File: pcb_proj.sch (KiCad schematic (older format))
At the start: 0 parts

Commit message: Mi-work push
Started dropping in the op-amps, still work in progress.
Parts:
- added R5: 1k, symbol R
- added U0, U1, U2, U3, U4, U5, U6, U7, U8, U9: OPA333xxDBV, symbol OPA333xxDBV
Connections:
- net labels added: GNDA, crossbar_out5, crossbar_out5_-v
- net labels removed: +12L
- wire segments 0 -> 8
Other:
- note added: "<--Ip--"
- note added: "Rf"
- note added: "Vout"
- note added: "Vout = Ip * Rf"
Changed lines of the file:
@@
 encoding utf-8
 Sheet 1 1
-Title ""
-Date ""
+Title "Operational Amplifiers"
+Date "2019-02-18"
 Rev ""
-Comp ""
+Comp "Emulating NN with Resistor Network"
 Comment1 ""
 Comment2 ""
@@
 $EndDescr
 $Comp
-L +12L #PWR?
-U 1 1 5C608EB0
-P 8050 2800
-F 0 "#PWR?" H 8050 2650 50  0001 C CNN
-F 1 "+12L" H 8050 2940 50  0000 C CNN
-F 2 "" H 8050 2800 50  0001 C CNN
-F 3 "" H 8050 2800 50  0001 C CNN
-	1    8050 2800
+L OPA333xxDBV U4
+U 1 1 5C6B1C00
+P 8750 3050
+F 0 "U4" H 8750 3250 50  0000 L CNN
+F 1 "OPA333xxDBV" H 8750 2850 50  0000 L CNN
+F 2 "" H 8750 3050 50  0001 C CNN
+F 3 "" H 8750 3250 50  0001 C CNN
+	1    8750 3050
 	1    0    0    -1
 $EndComp
+$Comp
+L OPA333xxDBV U5
+U 1 1 5C6B1C2C
+P 2500 4850
+F 0 "U5" H 2500 5050 50  0000 L CNN
+F 1 "OPA333xxDBV" H 2500 4650 50  0000 L CNN
+F 2 "" H 2500 4850 50  0001 C CNN
+F 3 "" H 2500 5050 50  0001 C CNN
+	1    2500 4850
+	1    0    0    -1
+$EndComp
+$Comp
+L OPA333xxDBV U7
+U 1 1 5C6B1C4E
+P 5500 4850
+F 0 "U7" H 5500 5050 50  0000 L CNN
+F 1 "OPA333xxDBV" H 5500 4650 50  0000 L CNN
+F 2 "" H 5500 4850 50  0001 C CNN
+F 3 "" H 5500 5050 50  0001 C CNN
+	1    5500 4850
+	1    0    0    -1
+$EndComp
+$Comp
+L OPA333xxDBV U9
+U 1 1 5C6B1C6F
+P 8750 4950
+F 0 "U9" H 8750 5150 50  0000 L CNN
+F 1 "OPA333xxDBV" H 8750 4750 50  0000 L CNN
+F 2 "" H 8750 4950 50  0001 C CNN
+F 3 "" H 8750 5150 50  0001 C CNN
+	1    8750 4950
+	1    0    0    -1
+$EndComp
+$Comp
+L OPA333xxDBV U2
+U 1 1 5C6B1C93
+P 5500 3000
+F 0 "U2" H 5500 3200 50  0000 L CNN
+F 1 "OPA333xxDBV" H 5500 2800 50  0000 L CNN
+F 2 "" H 5500 3000 50  0001 C CNN
+F 3 "" H 5500 3200 50  0001 C CNN
+	1    5500 3000
+	1    0    0    -1
+$EndComp
+$Comp
+L OPA333xxDBV U3
+U 1 1 5C6B1CC4
+P 7150 3000
+F 0 "U3" H 7150 3200 50  0000 L CNN
+F 1 "OPA333xxDBV" H 7150 2800 50  0000 L CNN
+F 2 "" H 7150 3000 50  0001 C CNN
+F 3 "" H 7150 3200 50  0001 C CNN
+	1    7150 3000
+	1    0    0    -1
+$EndComp
+$Comp
+L OPA333xxDBV U6
+U 1 1 5C6B1CF6
+P 4000 4850
+F 0 "U6" H 4000 5050 50  0000 L CNN
+F 1 "OPA333xxDBV" H 4000 4650 50  0000 L CNN
+F 2 "" H 4000 4850 50  0001 C CNN
+F 3 "" H 4000 5050 50  0001 C CNN
+	1    4000 4850
+	1    0    0    -1
+$EndComp
+$Comp
+L OPA333xxDBV U8
+U 1 1 5C6B1D2B
+P 7150 4850
+F 0 "U8" H 7150 5050 50  0000 L CNN
+F 1 "OPA333xxDBV" H 7150 4650 50  0000 L CNN
+F 2 "" H 7150 4850 50  0001 C CNN
+F 3 "" H 7150 5050 50  0001 C CNN
+	1    7150 4850
+	1    0    0    -1
+$EndComp
+$Comp
+L OPA333xxDBV U1
+U 1 1 5C6B1D5D
+P 4050 3000
+F 0 "U1" H 4050 3200 50  0000 L CNN
+F 1 "OPA333xxDBV" H 4050 2800 50  0000 L CNN
+F 2 "" H 4050 3000 50  0001 C CNN
+F 3 "" H 4050 3200 50  0001 C CNN
+	1    4050 3000
+	1    0    0    -1
+$EndComp
+$Comp
+L OPA333xxDBV U0
+U 1 1 5C6B1D94
+P 2500 3000
+F 0 "U0" H 2500 3200 50  0000 L CNN
+F 1 "OPA333xxDBV" H 2500 2800 50  0000 L CNN
+F 2 "" H 2500 3000 50  0001 C CNN
+F 3 "" H 2500 3200 50  0001 C CNN
+	1    2500 3000
+	1    0    0    -1
+$EndComp
+$Comp
+L GNDA #PWR?
+U 1 1 5C6B2BDA
+P 2200 5400
+F 0 "#PWR?" H 2200 5150 50  0001 C CNN
+F 1 "GNDA" H 2200 5250 50  0000 C CNN
+F 2 "" H 2200 5400 50  0001 C CNN
+F 3 "" H 2200 5400 50  0001 C CNN
+	1    2200 5400
+	1    0    0    -1
+$EndComp
+Wire Wire Line
+	2200 4950 2200 5400
+Text GLabel 1550 4750 0    60   Input ~ 0
+crossbar_out5
+$Comp
+L R R5
+U 1 1 5C6B34F2
+P 2250 4150
+F 0 "R5" V 2330 4150 50  0000 C CNN
+F 1 "1k" V 2250 4150 50  0000 C CNN
+F 2 "" V 2180 4150 50  0001 C CNN
+F 3 "" H 2250 4150 50  0001 C CNN
+	1    2250 4150
+	0    1    1    0
+$EndComp
+Wire Wire Line
+	1550 4750 2200 4750
+Wire Wire Line
+	1800 4750 1800 4150
+Wire Wire Line
+	1800 4150 2100 4150
+Connection ~ 1800 4750
+Wire Wire Line
+	2400 4150 2800 4150
+Wire Wire Line
+	2800 4150 2800 4850
+Wire Wire Line
+	2800 4850 3150 4850
+Wire Wire Line
+	3150 4850 3150 5350
+Connection ~ 2800 4850
+Text GLabel 3150 5350 0    60   Input ~ 0
+crossbar_out5_-v
+Text Notes 1150 4000 0    60   ~ 0
+Vout = Ip * Rf
+Text Notes 2950 4850 0    60   ~ 0
+Vout
+Text Notes 2500 4150 0    60   ~ 0
+Rf
+Text Notes 2050 4050 0    60   ~ 0
+<--Ip--
 $EndSCHEMATC

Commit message: About to make a heirarchy, committing first in case we need to go back
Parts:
- added R0, R1, R2, R3, R4, R6, R7, R8, R9: 1k, symbol R
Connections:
- net GNDA is gone; now on net GND: U5.4 (-)
- net crossbar_out4_-v: now reaches U4.1
- net crossbar_out4_-v: now also R4.1
- net crossbar_out3: now reaches U4.3 (+)
- net crossbar_out3: now also U3.3 (+), R3.2, R4.2
- net GND: now reaches U4.4 (-)
- net GND: now also U0.4 (-), U1.4 (-), U2.4 (-), U3.4 (-), U6.4 (-), U7.4 (-), U8.4 (-), U9.4 (-)
- net crossbar_out7_-v: now reaches U7.1
- net crossbar_out7_-v: now also R7.1
- net crossbar_out7: now reaches U7.3 (+)
- net crossbar_out7: now also R7.2
- net crossbar_out9_-v: now reaches U9.1
- net crossbar_out9_-v: now also R9.1
- net crossbar_out9: now reaches U9.3 (+)
- net crossbar_out9: now also R9.2
- net crossbar_out2_-v: now reaches U2.1
- net crossbar_out2_-v: now also R2.1
- net crossbar_out2: now reaches U2.3 (+)
- net crossbar_out2: now also R2.2
- net crossbar_out3_-v: now reaches U3.1
- net crossbar_out3_-v: now also R3.1
- net crossbar_out6_-v: now reaches U6.1
- net crossbar_out6_-v: now also R6.1
- net crossbar_out6: now reaches U6.3 (+)
- net crossbar_out6: now also R6.2
- net crossbar_out8_-v: now reaches U8.1
- net crossbar_out8_-v: now also R8.1
- net crossbar_out8: now reaches U8.3 (+)
- net crossbar_out8: now also R8.2
- net crossbar_out1_-v: now reaches U1.1
- net crossbar_out1_-v: now also R1.1
- net crossbar_out1: now reaches U1.3 (+)
- net crossbar_out1: now also R1.2
- net crossbar_out0_-v: now reaches U0.1
- net crossbar_out0_-v: now also R0.1
- net crossbar_out0: now reaches U0.3 (+)
- net crossbar_out0: now also R0.2
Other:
- note added: "This op amp is wired the same as the rest, just more\nexplicit in what's going on. Note the output voltage \nwill appear negative if the current is going INTO the \n1k resistor."
- moved on the sheet: R5, U0, U1, U2, U3, U4, U5, U6, U7, U8, U9

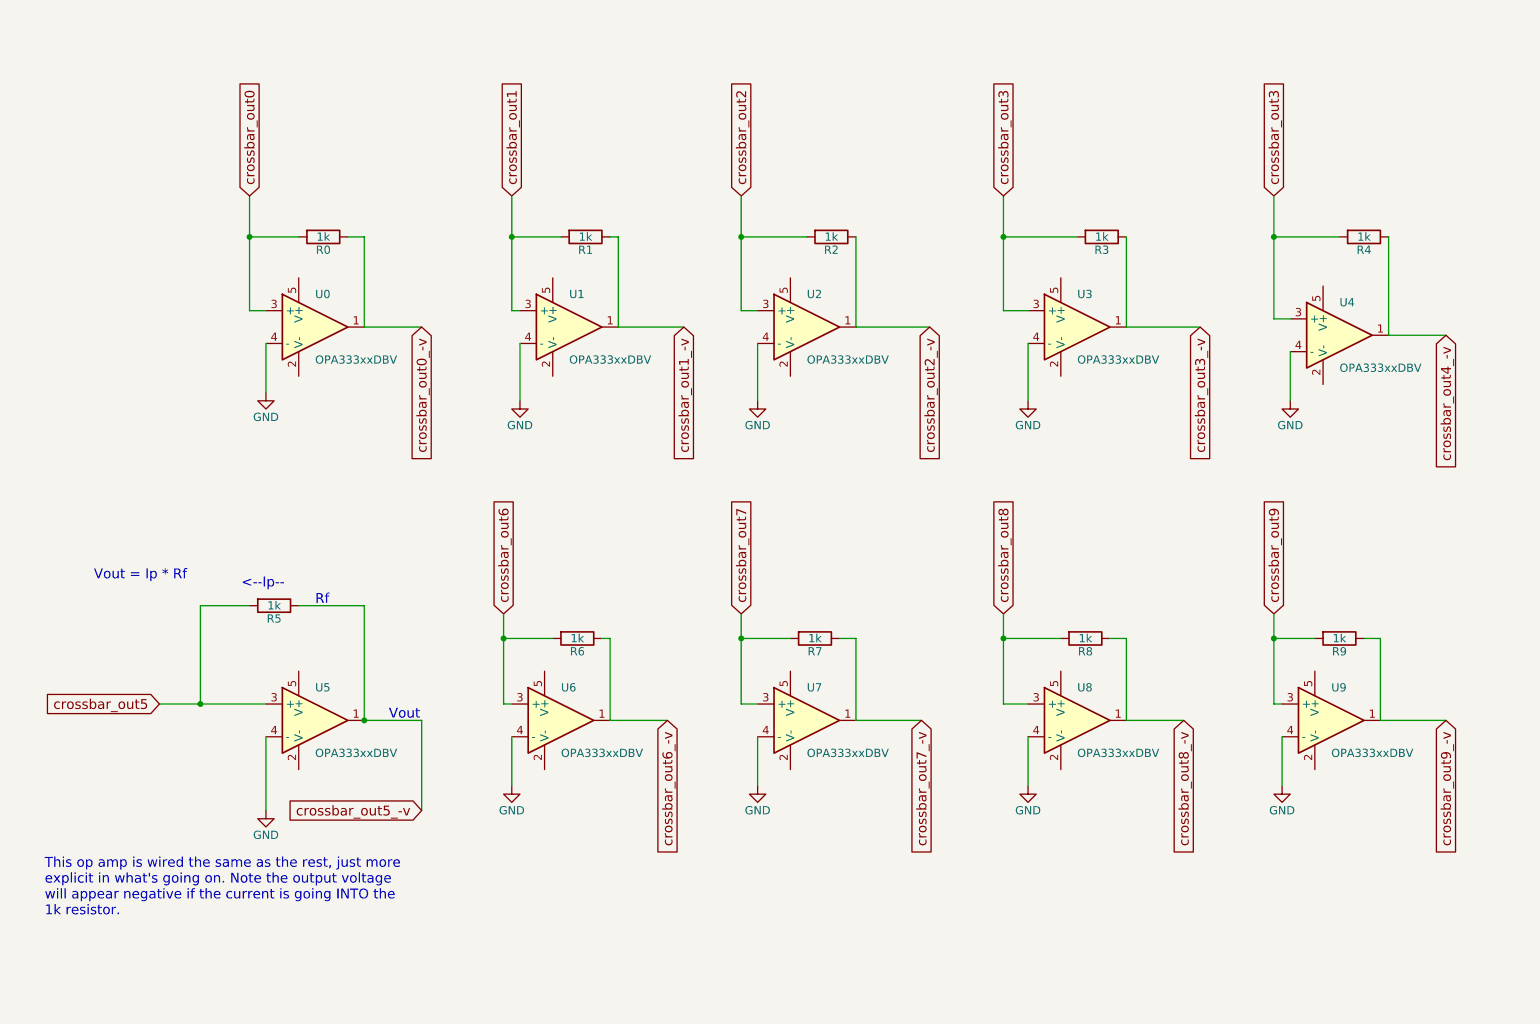
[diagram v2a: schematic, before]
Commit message: Start of Heirarchy
Placed the Op Amps into their own block (still need to 'hook up' output pins). Created block for resistor network.
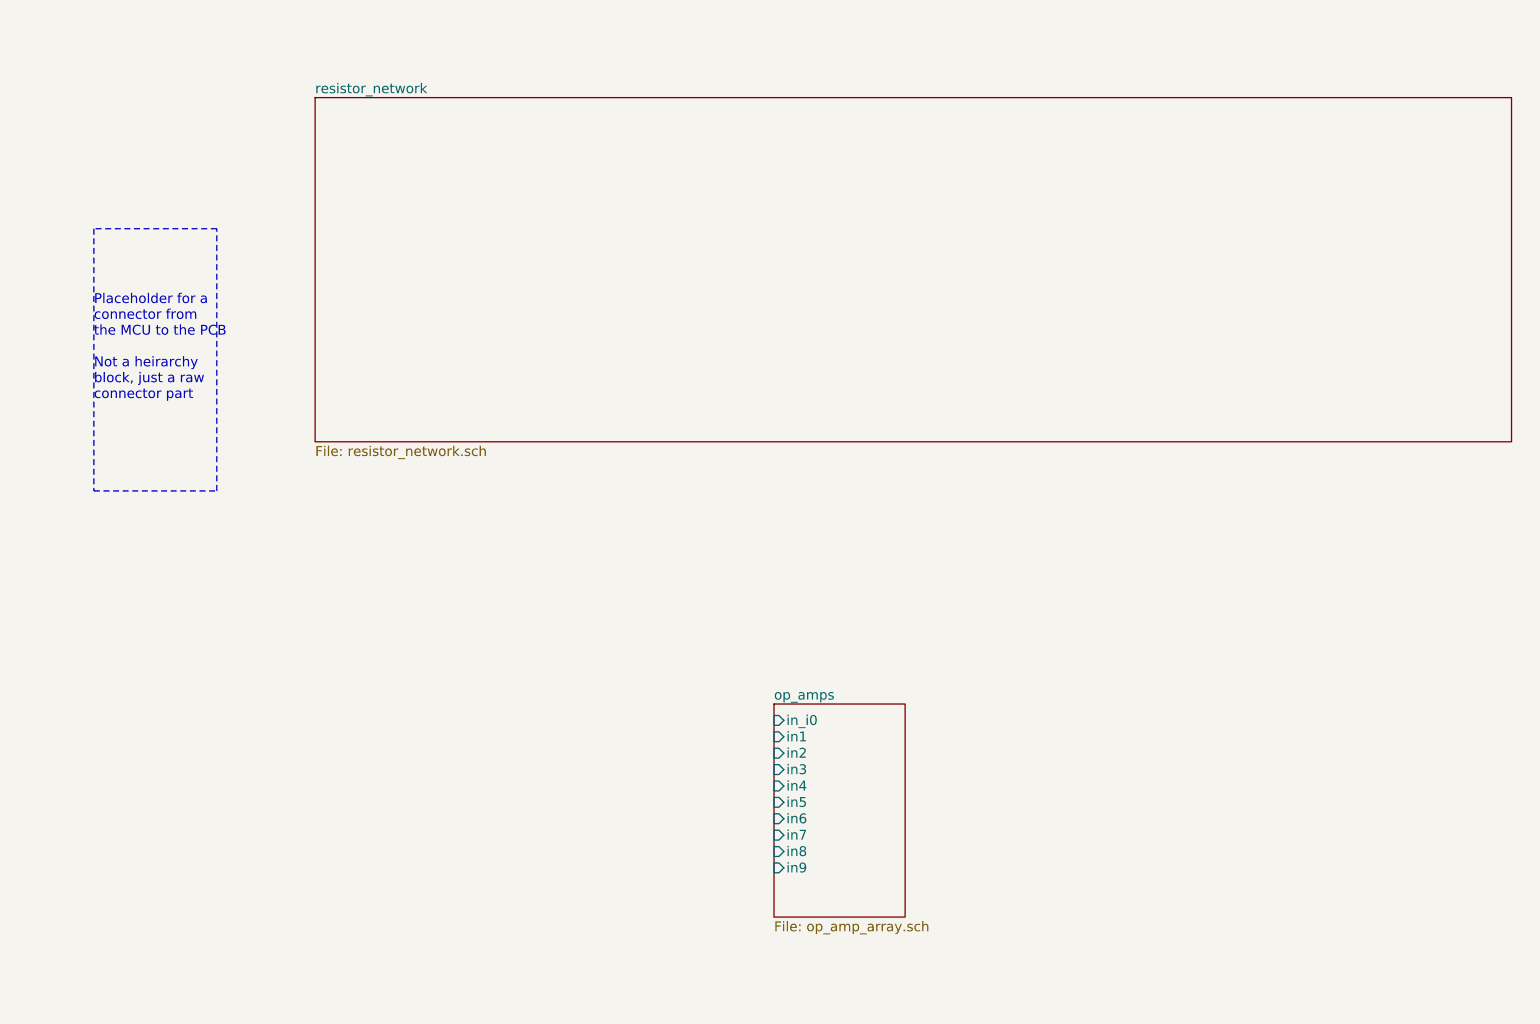
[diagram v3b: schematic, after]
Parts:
- removed R0, R1, R2, R3, R4, R5, R6, R7, R8, R9: 1k, symbol R
- removed U0, U1, U2, U3, U4, U5, U6, U7, U8, U9: OPA333xxDBV, symbol OPA333xxDBV
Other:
- note added: "Placeholder for a\nconnector from\nthe MCU to the PCB\n\nNot a heirarchy\nblock, just a raw\nconnector part"
- note removed: "<--Ip--"
- note removed: "Rf"
- note removed: "This op amp is wired the same as the rest, just more\nexplicit in what's going on. Note the output voltage \nwill appear negative if the current is going INTO the \n1k resistor."
- note removed: "Vout"
- note removed: "Vout = Ip * Rf"

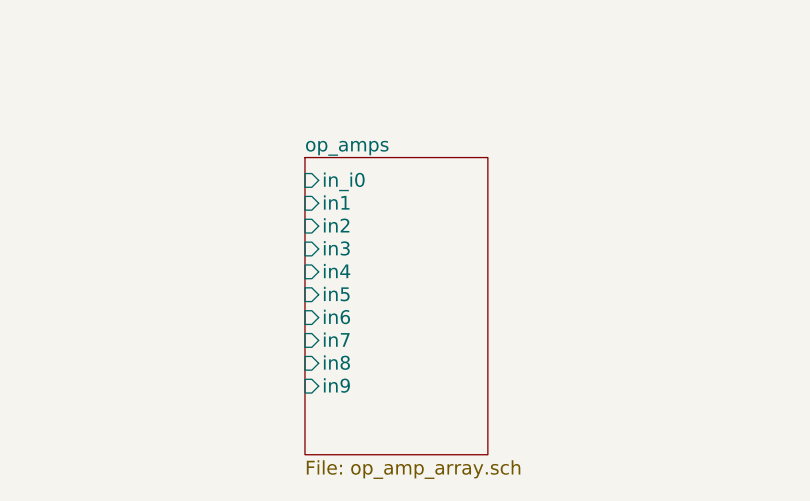
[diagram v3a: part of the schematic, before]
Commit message: Additional Heirarchy Changes
Added resistor pages, still need to update values on them. See weight matrix file.
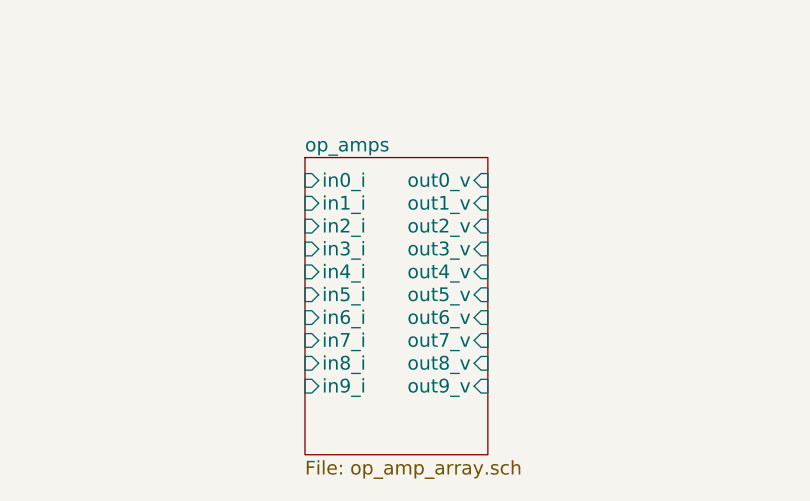
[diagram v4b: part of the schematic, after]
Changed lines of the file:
@@
 $Descr A4 11693 8268
 encoding utf-8
-Sheet 1 3
+Sheet 1 7
 Title "Operational Amplifiers"
 Date "2019-02-18"
@@
 F0 "op_amps" 60
 F1 "op_amp_array.sch" 60
-F2 "in_i0" I L 5300 5050 60
-F3 "in1" I L 5300 5150 60
-F4 "in2" I L 5300 5250 60
-F5 "in3" I L 5300 5350 60
-F6 "in4" I L 5300 5450 60
-F7 "in9" I L 5300 5950 60
-F8 "in8" I L 5300 5850 60
-F9 "in7" I L 5300 5750 60
-F10 "in6" I L 5300 5650 60
-F11 "in5" I L 5300 5550 60
+F2 "in0_i" I L 5300 5050 60
+F3 "in1_i" I L 5300 5150 60
+F4 "in2_i" I L 5300 5250 60
+F5 "in3_i" I L 5300 5350 60
+F6 "in4_i" I L 5300 5450 60
+F7 "in9_i" I L 5300 5950 60
+F8 "in8_i" I L 5300 5850 60
+F9 "in7_i" I L 5300 5750 60
+F10 "in6_i" I L 5300 5650 60
+F11 "in5_i" I L 5300 5550 60
+F12 "out0_v" I R 6100 5050 60
+F13 "out1_v" I R 6100 5150 60
+F14 "out2_v" I R 6100 5250 60
+F15 "out3_v" I R 6100 5350 60
+F16 "out4_v" I R 6100 5450 60
+F17 "out5_v" I R 6100 5550 60
+F18 "out6_v" I R 6100 5650 60
+F19 "out7_v" I R 6100 5750 60
+F20 "out8_v" I R 6100 5850 60
+F21 "out9_v" I R 6100 5950 60
 $EndSheet
 Wire Notes Line
